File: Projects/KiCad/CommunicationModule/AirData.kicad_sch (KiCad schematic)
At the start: 30 parts, among them J1 Conn_01x08, SW1 SW_Push, U1 MCP2562-E-P, U2 MCP2515-I/P, U3 NJM7805SDL1, U4 ABX00012, Y1 8MHz

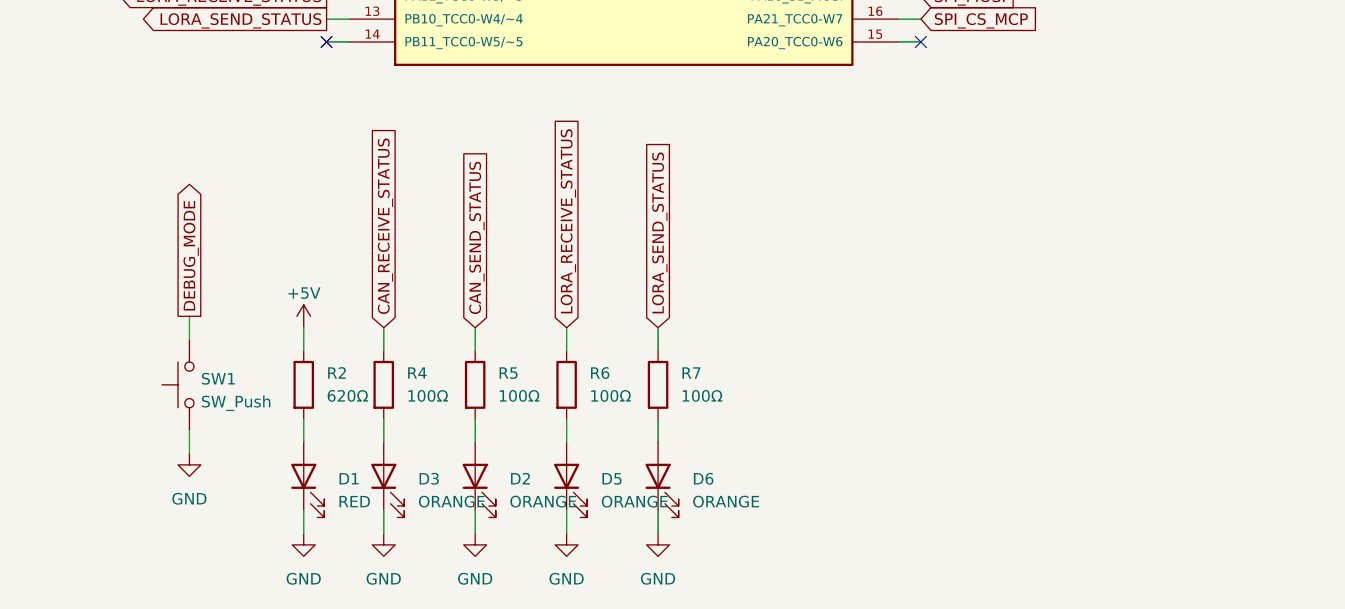
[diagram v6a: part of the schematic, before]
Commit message: スイッチをピアノスイッチに変更
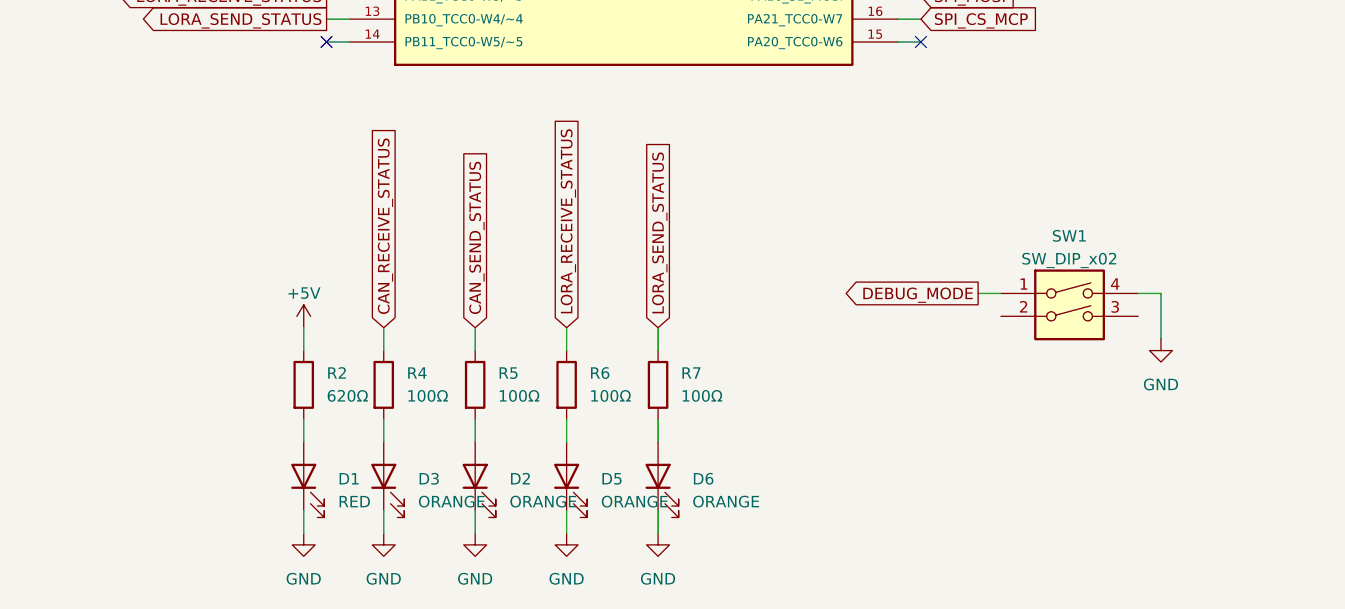
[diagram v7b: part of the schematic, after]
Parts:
- removed SW1: SW_Push, Button_Switch_THT:SW_PUSH_6mm, symbol Switch:SW_Push
- added SW1: SW_DIP_x02, Button_Switch_THT:SW_DIP_SPSTx02_Piano_10.8x6.64mm_W7.62mm_P2.54mm, symbol Switch:SW_DIP_x02
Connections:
- net DEBUG_MODE: now also SW1.1
- net GND: now also SW1.4
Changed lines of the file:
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@@
+    (stroke (width 0) (type default))
+  )
+  (wire (pts (xy 149.86 156.21) (xy 149.86 161.29))
     (stroke (width 0) (type default))
   )
@@
     (stroke (width 0) (type default))
   )
-  (wire (pts (xy 41.91 158.75) (xy 41.91 161.29))
-    (stroke (width 0) (type default))
-  )
   (wire (pts (xy 105.41 63.5) (xy 105.41 66.04))
     (stroke (width 0) (type default))
@@
     (stroke (width 0) (type default))
   )
+  (wire (pts (xy 129.54 156.21) (xy 132.08 156.21))
+    (stroke (width 0) (type default))
+  )
   (wire (pts (xy 33.02 30.48) (xy 33.02 29.21))
     (stroke (width 0) (type default))
@@
     (stroke (width 0) (type default))
   )
+  (wire (pts (xy 147.32 156.21) (xy 149.86 156.21))
+    (stroke (width 0) (type default))
+  )
   (wire (pts (xy 125.73 97.79) (xy 120.65 97.79))
     (stroke (width 0) (type default))
@@
   )
   (wire (pts (xy 93.98 180.34) (xy 93.98 182.88))
-    (stroke (width 0) (type default))
-  )
-  (wire (pts (xy 41.91 171.45) (xy 41.91 173.99))
     (stroke (width 0) (type default))
   )
@@
     )
   )
+  (global_label "DEBUG_MODE" (shape output) (at 129.54 156.21 180) (fields_autoplaced)
+    (effects (font (size 1.27 1.27)) (justify right))
+    (property "Intersheetrefs" "${INTERSHEET_REFS}" (at 114.1762 156.21 0)
+      (effects (font (size 1.27 1.27)) (justify right) hide)
+    )
+  )
   (global_label "CAN_H" (shape bidirectional) (at 34.29 53.34 180) (fields_autoplaced)
     (effects (font (size 1.27 1.27)) (justify right))
@@
     )
   )
-  (global_label "DEBUG_MODE" (shape output) (at 41.91 158.75 90) (fields_autoplaced)
-    (effects (font (size 1.27 1.27)) (justify left))
-    (property "Intersheetrefs" "${INTERSHEET_REFS}" (at 41.91 143.3862 90)
-      (effects (font (size 1.27 1.27)) (justify left) hide)
-    )
-  )
   (global_label "LORA_RECEIVE_STATUS" (shape input) (at 83.82 160.02 90) (fields_autoplaced)
     (effects (font (size 1.27 1.27)) (justify left))
@@
     )
   )
+  (symbol (lib_id "Switch:SW_DIP_x02") (at 139.7 158.75 0) (unit 1)
+    (in_bom yes) (on_board yes) (dnp no) (fields_autoplaced)
+    (property "Reference" "SW1" (at 139.7 149.86 0)
+      (effects (font (size 1.27 1.27)))
+    )
+    (property "Value" "SW_DIP_x02" (at 139.7 152.4 0)
+      (effects (font (size 1.27 1.27)))
+    )
+    (property "Footprint" "Button_Switch_THT:SW_DIP_SPSTx02_Piano_10.8x6.64mm_W7.62mm_P2.54mm" (at 139.7 158.75 0)
+      (effects (font (size 1.27 1.27)) hide)
+    )
+    (property "Datasheet" "~" (at 139.7 158.75 0)
+      (effects (font (size 1.27 1.27)) hide)
+    )
+    (pin "1")
+    (pin "2")
+    (pin "3")
+    (pin "4")
+    (instances
+      (project "AirData"
+        (path "/ea1ed597-7cd3-4340-902e-bdce8f2d7a62"
+          (reference "SW1") (unit 1)
+        )
+      )
+    )
+  )
   (symbol (lib_id "power:+5V") (at 234.95 100.33 0) (unit 1)
     (in_bom yes) (on_board yes) (dnp no) (fields_autoplaced)
@@
         (path "/ea1ed597-7cd3-4340-902e-bdce8f2d7a62"
           (reference "R4") (unit 1)
+        )
+      )
+    )
+  )
+  (symbol (lib_id "power:GND") (at 149.86 161.29 0) (mirror y) (unit 1)
+    (in_bom yes) (on_board yes) (dnp no) (fields_autoplaced)
+    (property "Reference" "#PWR018" (at 149.86 167.64 0)
+      (effects (font (size 1.27 1.27)) hide)
+    )
+    (property "Value" "GND" (at 149.86 166.37 0)
+      (effects (font (size 1.27 1.27)))
+    )
+    (property "Footprint" "" (at 149.86 161.29 0)
+      (effects (font (size 1.27 1.27)) hide)
+    )
+    (property "Datasheet" "" (at 149.86 161.29 0)
+      (effects (font (size 1.27 1.27)) hide)
+    )
+    (pin "1")
+    (instances
+      (project "AirData"
+        (path "/ea1ed597-7cd3-4340-902e-bdce8f2d7a62"
+          (reference "#PWR018") (unit 1)
         )
       )
@@
         (path "/ea1ed597-7cd3-4340-902e-bdce8f2d7a62"
           (reference "#PWR03") (unit 1)
-        )
-      )
-    )
-  )
-  (symbol (lib_id "power:GND") (at 41.91 173.99 0) (mirror y) (unit 1)
-    (in_bom yes) (on_board yes) (dnp no) (fields_autoplaced)
-    (property "Reference" "#PWR018" (at 41.91 180.34 0)
-      (effects (font (size 1.27 1.27)) hide)
-    )
-    (property "Value" "GND" (at 41.91 179.07 0)
-      (effects (font (size 1.27 1.27)))
-    )
-    (property "Footprint" "" (at 41.91 173.99 0)
-      (effects (font (size 1.27 1.27)) hide)
-    )
-    (property "Datasheet" "" (at 41.91 173.99 0)
-      (effects (font (size 1.27 1.27)) hide)
-    )
-    (pin "1")
-    (instances
-      (project "AirData"
-        (path "/ea1ed597-7cd3-4340-902e-bdce8f2d7a62"
-          (reference "#PWR018") (unit 1)
         )
       )
@@
         )
       )
-    )
-  )
-  (symbol (lib_id "Switch:SW_Push") (at 41.91 166.37 90) (unit 1)
-    (in_bom yes) (on_board yes) (dnp no) (fields_autoplaced)
-    (property "Reference" "SW1" (at 43.18 165.735 90)
-      (effects (font (size 1.27 1.27)) (justify right))
-    )
-    (property "Value" "SW_Push" (at 43.18 168.275 90)
-      (effects (font (size 1.27 1.27)) (justify right))
-    )
-    (property "Footprint" "Button_Switch_THT:SW_PUSH_6mm" (at 36.83 166.37 0)
-      (effects (font (size 1.27 1.27)) hide)
-    )
-    (property "Datasheet" "~" (at 36.83 166.37 0)
-      (effects (font (size 1.27 1.27)) hide)
-    )
-    (pin "1")
-    (pin "2")
-    (instances
-      (project "AirData"
-        (path "/ea1ed597-7cd3-4340-902e-bdce8f2d7a62"
-          (reference "SW1") (unit 1)
-        )
-      )

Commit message: 三端子レギュレータをTO-252-3からTO-252-2に変更
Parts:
- U3: footprint Package_TO_SOT_SMD:TO-252-3_TabPin2 -> Package_TO_SOT_SMD:TO-252-2
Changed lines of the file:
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@@
       (effects (font (size 1.27 1.27)))
     )
-    (property "Footprint" "Package_TO_SOT_SMD:TO-252-3_TabPin2" (at 210.185 106.68 0)
+    (property "Footprint" "Package_TO_SOT_SMD:TO-252-2" (at 210.185 106.68 0)
       (effects (font (size 1.27 1.27) italic) (justify left) hide)
     )
